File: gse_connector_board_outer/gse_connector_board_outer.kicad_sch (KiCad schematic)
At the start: 10 parts, among them J1 arming_connector, J2 gse_com_connector, J3 chg_connector, J5 Conn_02x02_Top_Bottom, J6 Conn_02x02_Top_Bottom, J7 Conn_02x02_Top_Bottom, J8 GSE_cable, U1 ICS_CAN_Isolator

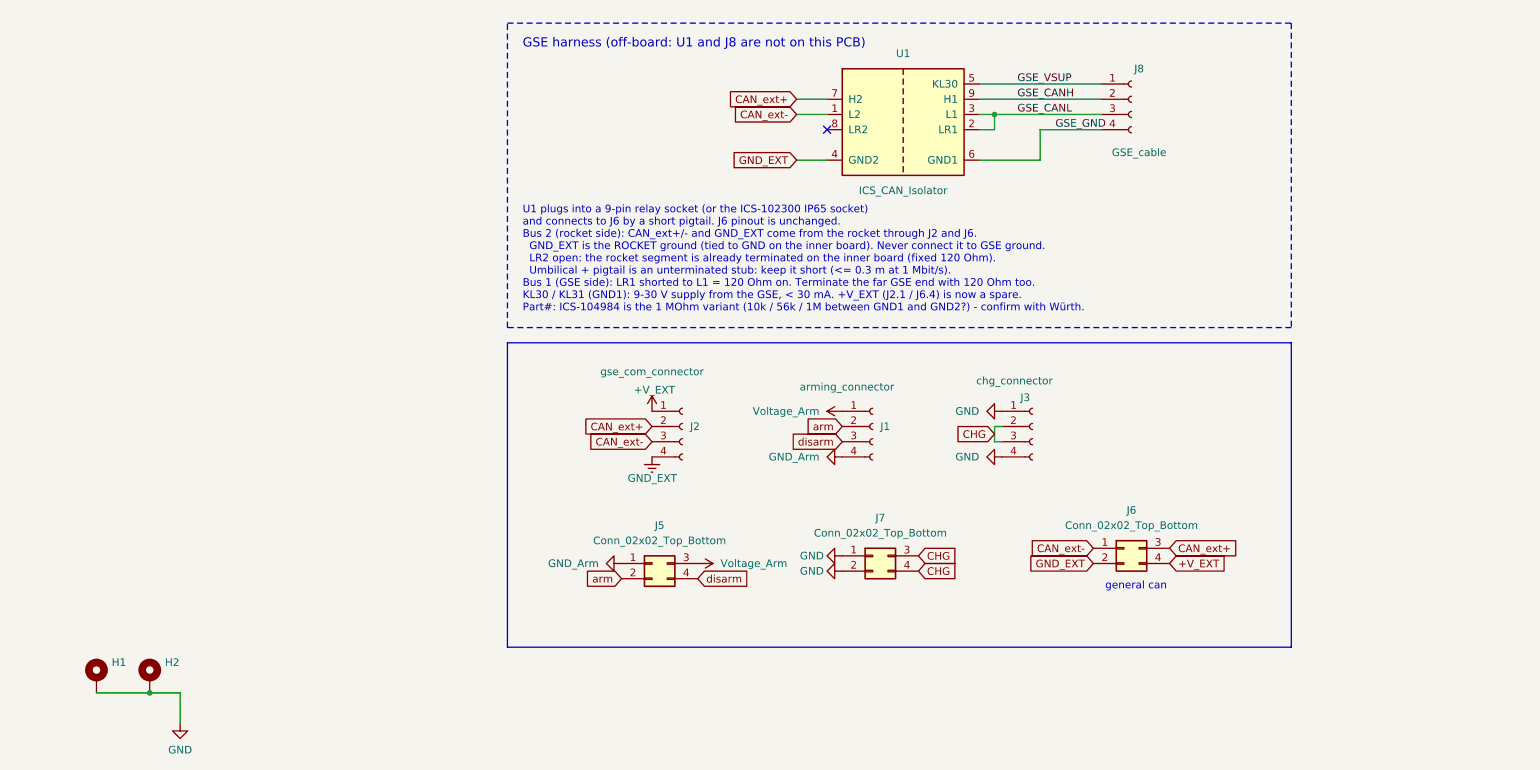
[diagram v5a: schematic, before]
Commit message: route new can isolation
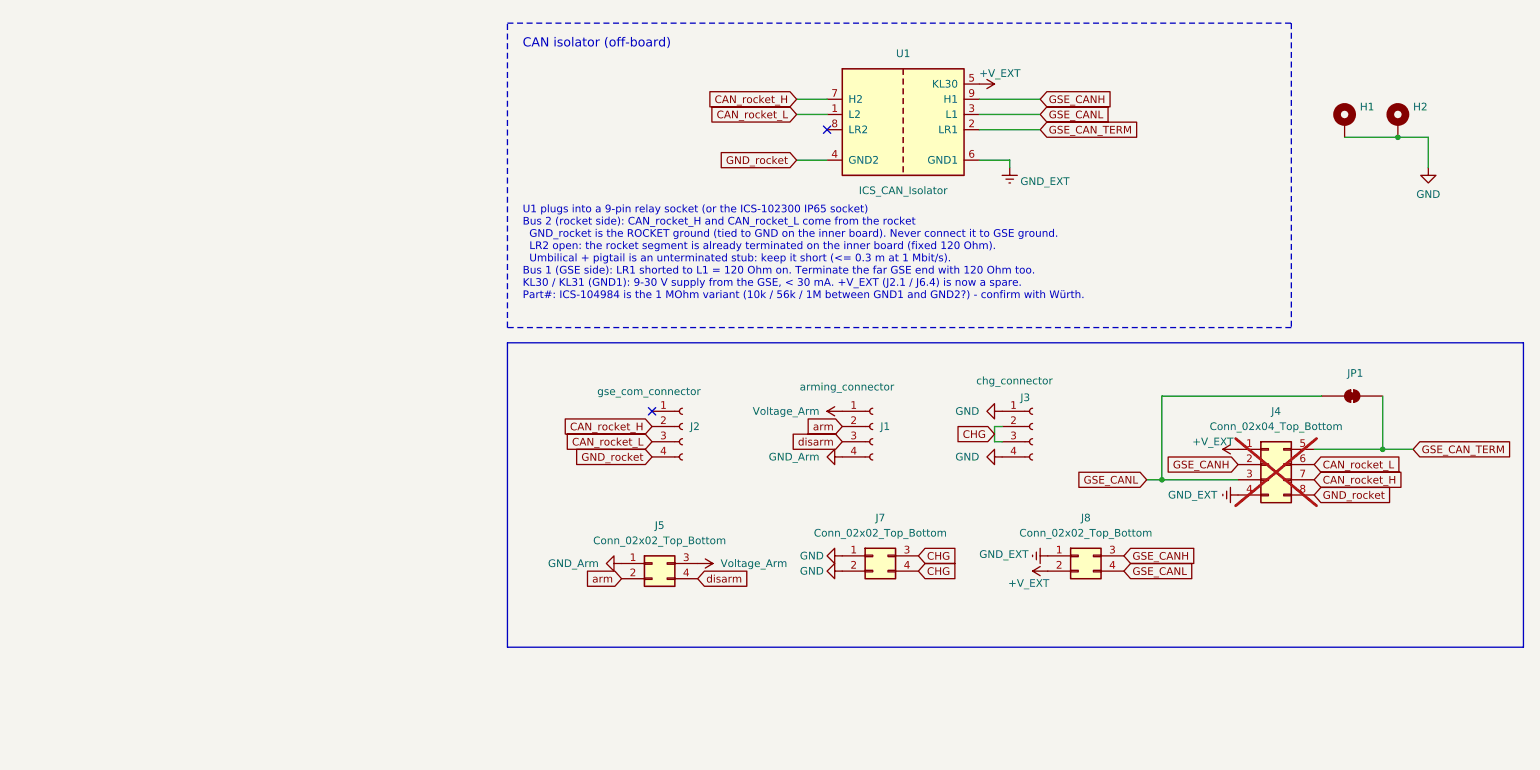
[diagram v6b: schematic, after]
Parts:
- removed J6: Conn_02x02_Top_Bottom, Connector_Molex:Molex_Micro-Fit_3.0_43045-0400_2x02_P3.00mm_Horizontal, symbol Connector_Generic:Conn_02x02_Top_Bottom
- removed J8: GSE_cable, symbol Connector:Conn_01x04_Socket
- added J4: Conn_02x04_Top_Bottom, Connector_Molex:Molex_Micro-Fit_3.0_43045-0800_2x04_P3.00mm_Horizontal, symbol Connector_Generic:Conn_02x04_Top_Bottom
- added J8: Conn_02x02_Top_Bottom, Connector_Molex:Molex_Micro-Fit_3.0_43045-0400_2x02_P3.00mm_Horizontal, symbol Connector_Generic:Conn_02x02_Top_Bottom
- added JP1: SolderJumper_2_Bridged, Jumper:SolderJumper-2_P1.3mm_Bridged_RoundedPad1.0x1.5mm, symbol Jumper:SolderJumper_2_Bridged
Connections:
- net GSE_GND is gone; now on net GND_EXT: U1.6 (GND1)
- net GSE_VSUP is gone; now on net +V_EXT: U1.5 (KL30)
- net +V_EXT: now also J4.1 (Pin_1), J8.2 (Pin_2); no longer J2.1 (Pin_1)
- net GND_EXT: now also J4.4 (Pin_4), J8.1 (Pin_1); no longer J2.4 (Pin_4), U1.4 (GND2)
- net GSE_CANH: now also J4.2 (Pin_2), J8.3 (Pin_3)
- net GSE_CANL: now also J4.3 (Pin_3), J8.4 (Pin_4), JP1.2 (B); no longer U1.2 (LR1)
- net CAN_ext+ renamed CAN_rocket_H
- net CAN_rocket_H: now also J4.7 (Pin_7)
- net CAN_ext- renamed CAN_rocket_L
- net CAN_rocket_L: now also J4.6 (Pin_6)
- new net GND_rocket: J2.4 (Pin_4), J4.8 (Pin_8), U1.4 (GND2)
- new net GSE_CAN_TERM: J4.5 (Pin_5), JP1.1 (A), U1.2 (LR1)
- no-connect marks 1 -> 2
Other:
- note added: "CAN isolator (off-board)"
- note added: "U1 plugs into a 9-pin relay socket (or the ICS-102300 IP65 socket) Bus 2 (rocket side): CAN_rocket_H and CAN_rocket_L come from the rocket GND_rocket is the ROCKET ground (tied to GND on the inner board). Never connect it to GSE ground. LR2 open: the rocket segment is already terminated on the inner board (fixed 120 Ohm). Umbilical + pigtail is an unterminated stub: keep it short (<= 0.3 m at 1 M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"
- note removed: "GSE harness (off-board: U1 and J8 are not on this PCB)"
- note removed: "U1 plugs into a 9-pin relay socket (or the ICS-102300 IP65 socket) and connects to J6 by a short pigtail. J6 pinout is unchanged. Bus 2 (rocket side): CAN_ext+/- and GND_EXT come from the rocket through J2 and J6. GND_EXT is the ROCKET ground (tied to GND on the inner board). Never connect it to GSE ground. LR2 open: the rocket segment is already terminated on the inner board (fixed 120 Ohm). Umb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"
- note removed: "general can"
- moved on the sheet: H1, H2

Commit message: adapted footprint again
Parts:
- J1, J2, J3: footprint custom_parts:4_pin_mag_con_new -> custom_parts:4_pin_mag_con_mv_adapt
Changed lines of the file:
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@@
 			)
 		)
-		(property "Footprint" "custom_parts:4_pin_mag_con_new"
+		(property "Footprint" "custom_parts:4_pin_mag_con_mv_adapt"
 			(at 181.61 82.55 0)
 			(hide yes)
@@
 			)
 		)
-		(property "Footprint" "custom_parts:4_pin_mag_con_new"
+		(property "Footprint" "custom_parts:4_pin_mag_con_mv_adapt"
 			(at 154.94 82.55 0)
 			(hide yes)
@@
 			)
 		)
-		(property "Footprint" "custom_parts:4_pin_mag_con_new"
+		(property "Footprint" "custom_parts:4_pin_mag_con_mv_adapt"
 			(at 123.19 82.55 0)
 			(hide yes)

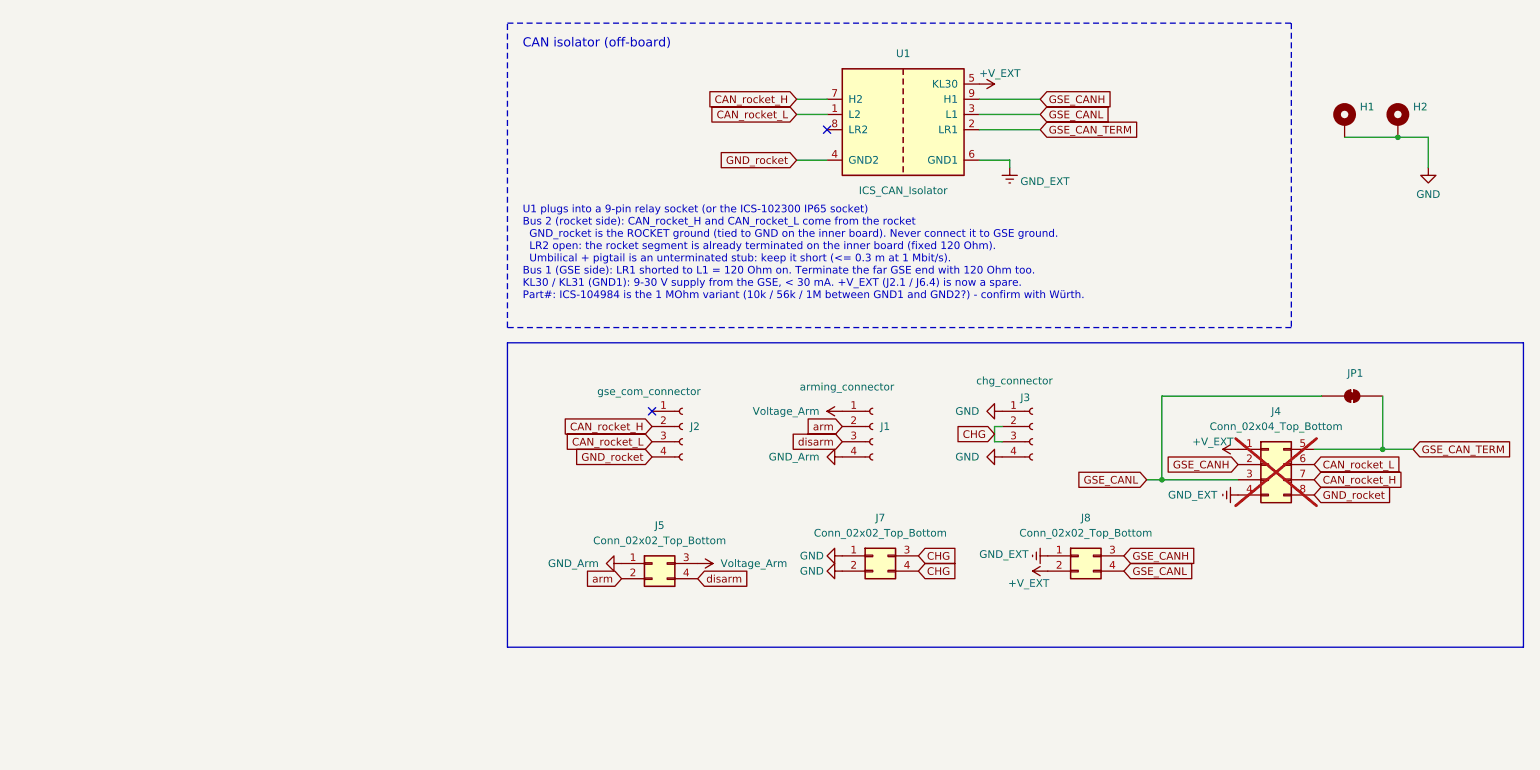
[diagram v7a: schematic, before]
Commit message: implement photoNMOS switch
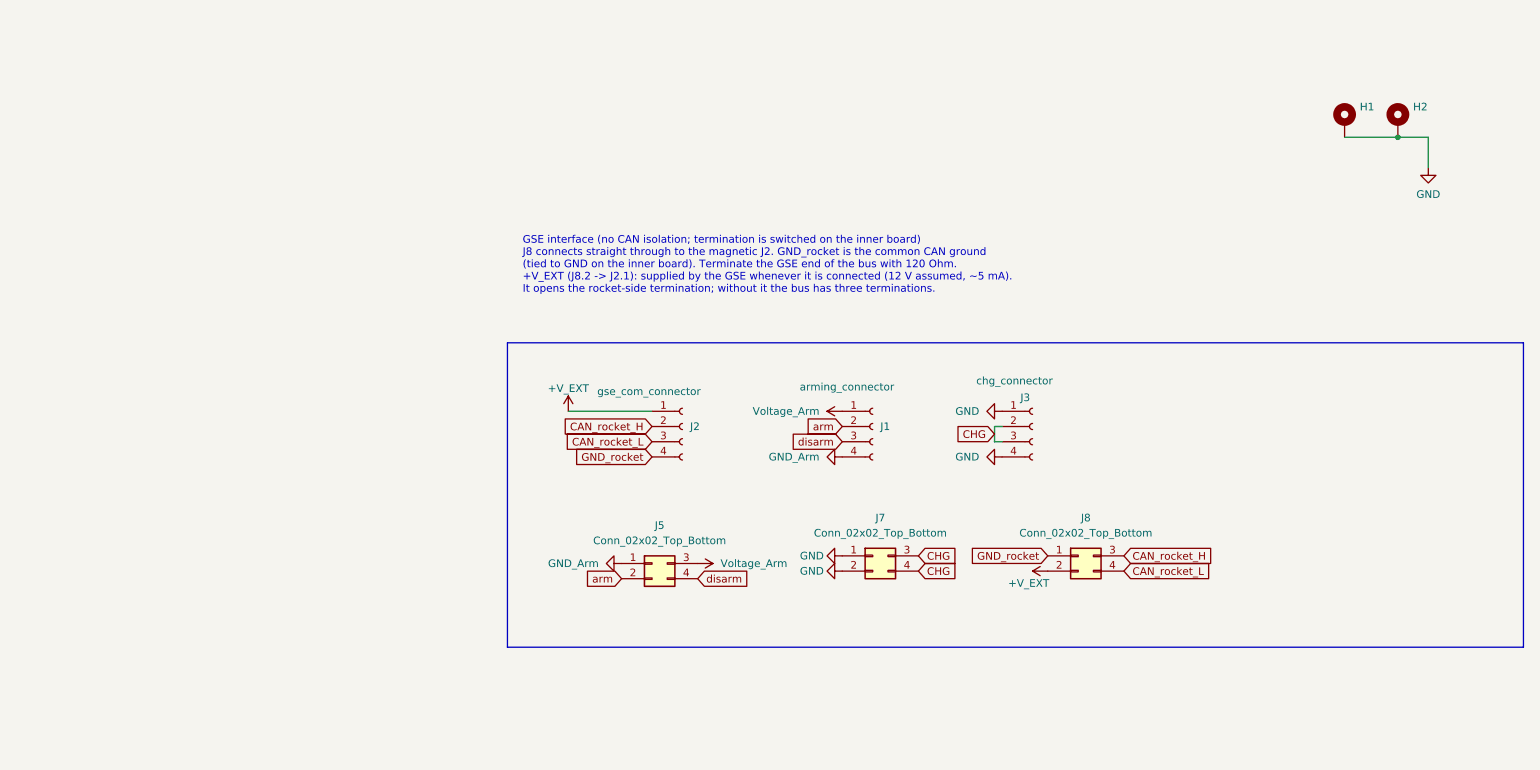
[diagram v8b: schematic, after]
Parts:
- removed J4: Conn_02x04_Top_Bottom, Connector_Molex:Molex_Micro-Fit_3.0_43045-0800_2x04_P3.00mm_Horizontal, symbol Connector_Generic:Conn_02x04_Top_Bottom
- removed JP1: SolderJumper_2_Bridged, Jumper:SolderJumper-2_P1.3mm_Bridged_RoundedPad1.0x1.5mm, symbol Jumper:SolderJumper_2_Bridged
- removed U1: ICS_CAN_Isolator, symbol custom_parts:ICS_CAN_Isolator
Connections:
- net GND_EXT is gone; now on net GND_rocket: J8.1 (Pin_1)
- net GSE_CANH is gone; now on net CAN_rocket_H: J8.3 (Pin_3)
- net GSE_CANL is gone; now on net CAN_rocket_L: J8.4 (Pin_4)
- net +V_EXT: now also J2.1 (Pin_1)
- no-connect marks 2 -> 0
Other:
- note added: "GSE interface (no CAN isolation; termination is switched on the inner board) J8 connects straight through to the magnetic J2. GND_rocket is the common CAN ground (tied to GND on the inner board). Terminate the GSE end of the bus with 120 Ohm. +V_EXT (J8.2 -> J2.1): supplied by the GSE whenever it is connected (12 V assumed, ~5 mA). It opens the rocket-side termination; without it the bus has thre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"
- note removed: "CAN isolator (off-board)"
- note removed: "U1 plugs into a 9-pin relay socket (or the ICS-102300 IP65 socket) Bus 2 (rocket side): CAN_rocket_H and CAN_rocket_L come from the rocket GND_rocket is the ROCKET ground (tied to GND on the inner board). Never connect it to GSE ground. LR2 open: the rocket segment is already terminated on the inner board (fixed 120 Ohm). Umbilical + pigtail is an unterminated stub: keep it short (<= 0.3 m at 1 M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"
